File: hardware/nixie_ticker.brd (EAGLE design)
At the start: 127 x 61 mm, 78 parts, among them Q1 BCX19SMD, Q2 BCX19SMD, U1 K155ID1, U2 K155ID1, U3 K155ID1, U4 K155ID1, U5 K155ID1, U6 K155ID1

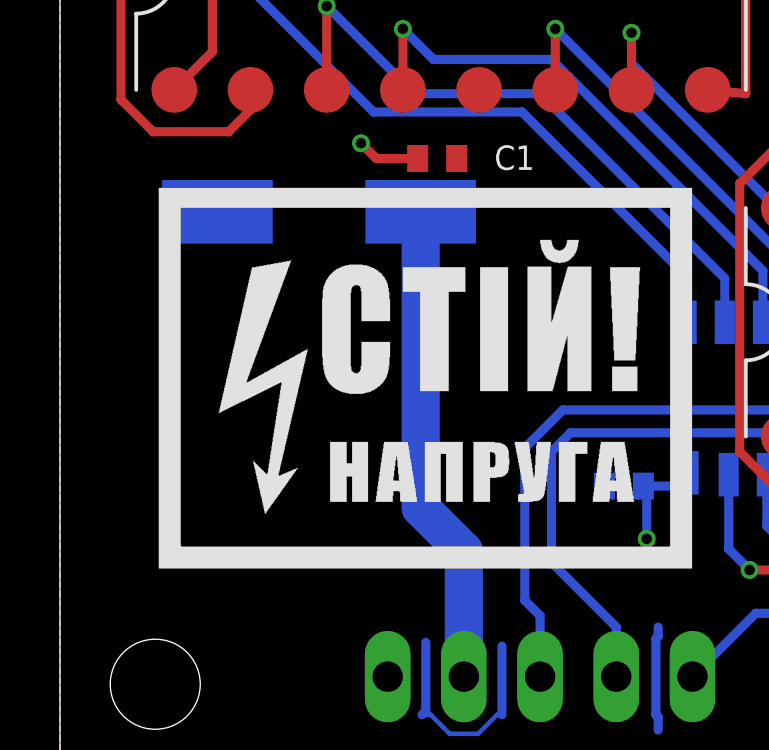
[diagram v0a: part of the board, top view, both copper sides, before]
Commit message: Changing OSH logo on power supply
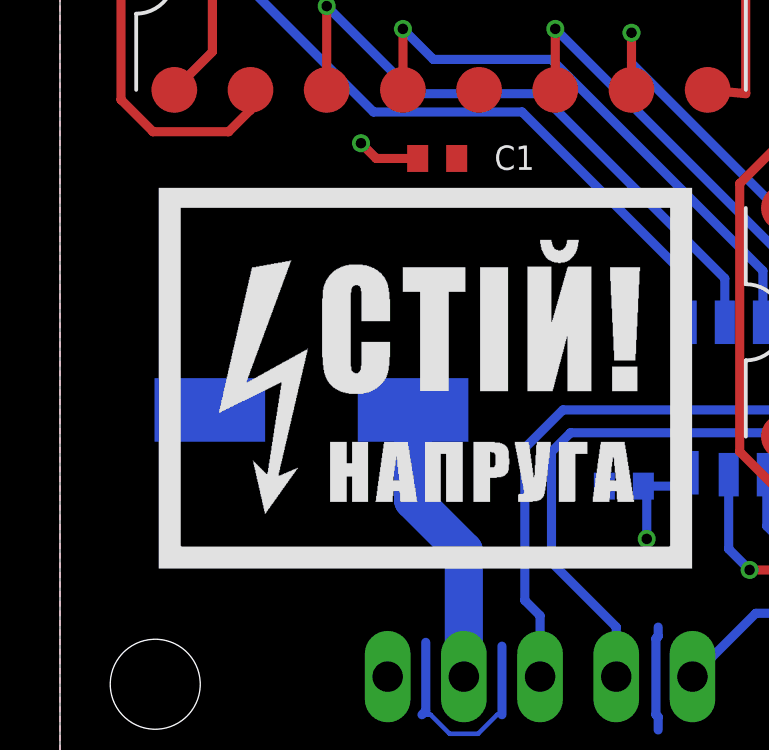
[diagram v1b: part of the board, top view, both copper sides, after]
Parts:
- moved C15 6.61 mm to (8.38, 12.3)
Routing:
- net +5V: track 38.8 -> 32.3 mm
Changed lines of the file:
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@@
 <attribute name="VALUE" x="80.01" y="5.207" size="1.27" layer="28" rot="MR90"/>
 </element>
-<element name="C15" library="nixie_ticker" library_urn="urn:adsk.eagle:library:3857935" package="CAPAE830X1050" package3d_urn="urn:adsk.eagle:package:3945414/1" value="220uF" x="8.636" y="18.923" rot="MR0"/>
+<element name="C15" library="nixie_ticker" library_urn="urn:adsk.eagle:library:3857935" package="CAPAE830X1050" package3d_urn="urn:adsk.eagle:package:3945414/1" value="220uF" x="8.382" y="12.319" rot="MR0"/>
 <element name="JP2" library="pinhead" library_urn="urn:adsk.eagle:library:325" package="1X05" package3d_urn="urn:adsk.eagle:package:22469/2" value="" x="16.002" y="3.429" smashed="yes" rot="MR180">
 <attribute name="VALUE" x="9.652" y="6.604" size="1.27" layer="28" rot="MR180"/>
@@
 <contactref element="C15" pad="1"/>
 <contactref element="JP2" pad="2"/>
-<wire x1="12.0237" y1="18.923" x2="12.0237" y2="9.0583" width="1.27" layer="16"/>
+<wire x1="11.7697" y1="12.319" x2="11.7697" y2="9.3123" width="1.27" layer="16"/>
 <wire x1="13.462" y1="7.62" x2="13.462" y2="3.429" width="1.27" layer="16"/>
-<wire x1="12.0237" y1="9.0583" x2="13.462" y2="7.62" width="1.27" layer="16"/>
+<wire x1="11.7697" y1="9.3123" x2="13.462" y2="7.62" width="1.27" layer="16"/>
 <wire x1="71.755" y1="10.225" x2="70.674" y2="9.144" width="0.3048" layer="16"/>
 <wire x1="69.992" y1="9.144" x2="68.468" y2="10.668" width="0.3048" layer="16"/>

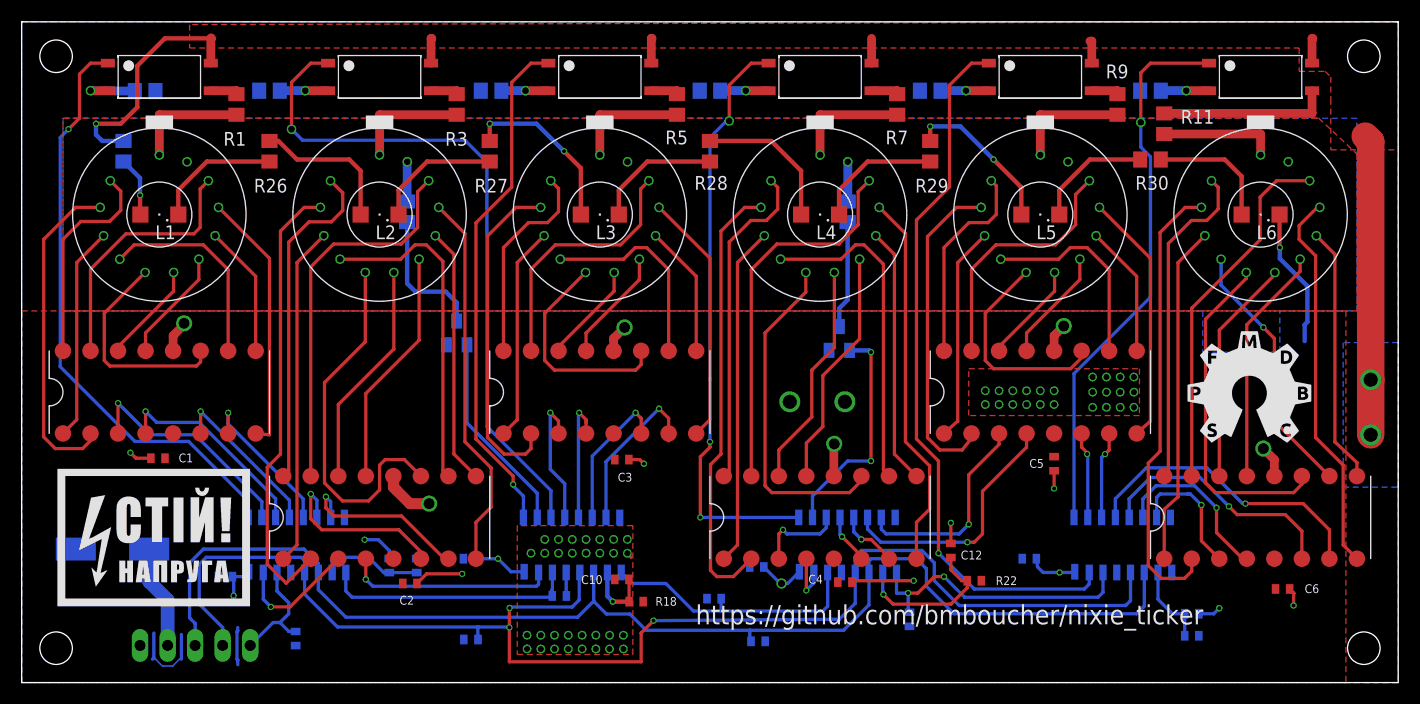
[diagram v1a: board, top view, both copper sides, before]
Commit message: Updates 8-17, adding fifth shift register
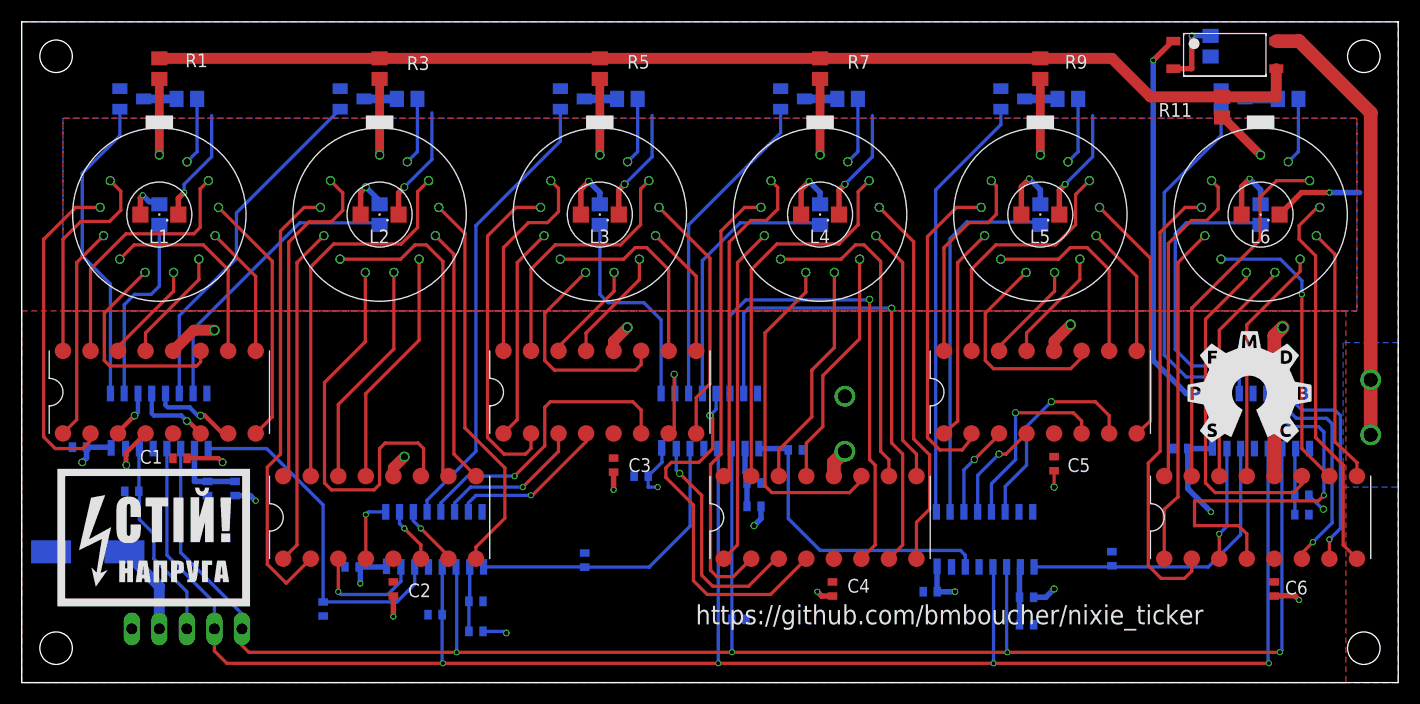
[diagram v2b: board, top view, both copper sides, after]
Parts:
- removed U$14, U$18, U$21, U$22, U$23: TLP3873D, nixie_ticker:SOP254P1000X215-4
- added C16, C17: (no value), resistor:C0402
- added Q3, Q4, Q5, Q6: BCX19SMD, transistor-npn:SOT23-BEC
- added R31: (no value), resistor:R0402
- added U$1: 74AHC595, nixie_ticker:16SOIC
- R12: device resistor:R0805 -> resistor:R0402
- moved R2 98.4 mm to (109.7, 58.7), turned to 90 degrees
- moved U$13 98.3 mm to (111.0, 57.9)
- moved R12 39.9 mm to (118.1, 17.3)
- moved R10 33.0 mm to (116.8, 53.8)
- moved R8 33.0 mm to (96.5, 53.8)
- moved Q1 23.6 mm to (30.5, 53.8), turned to 90 degrees
- moved Q2 22.5 mm to (71.1, 53.8), turned to 90 degrees
- moved R17 21.8 mm to (27.8, 6.79), turned to 90 degrees
- moved R22 21.4 mm to (67.6, 16.3), flipped to the bottom, turned to 180 degrees
- moved C8 20.6 mm to (17.1, 17.9), turned to 270 degrees
- moved R16 20.3 mm to (10.2, 17.7), turned to 180 degrees
- moved C12 19.2 mm to (67.6, 18.4), flipped to the bottom, turned to 180 degrees
- moved R23 18.8 mm to (71.4, 21.5), turned to 0 degrees
- moved C7 18.0 mm to (5.33, 21.7)
- moved U$3 17.1 mm to (12.7, 24.1)
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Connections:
- removed net D1A: U$13.1, U$3.P$1
- removed net D2A: U$14.1, U$4.P$3
- removed net D3A: U$18.1, U$4.P$1
- removed net D4A: U$21.1, U$9.P$1
- removed net D5A: U$10.P$15, U$22.1
- removed net D6A: U$10.P$1, U$23.1
- removed net N$106: R3.2, U$14.3
- removed net N$107: R4.2, U$14.2
- removed net N$112: R5.2, U$18.3
- removed net N$113: R6.2, U$18.2
- removed net N$119: R7.2, U$21.3
- removed net N$120: R8.2, U$21.2
- removed net N$146: R9.2, U$22.3
- removed net N$147: R10.2, U$22.2
- removed net N$153: R11.2, U$23.3
- removed net N$154: R12.2, U$23.2
- removed net N$28: L3.C, R28.1
- removed net N$41: L4.C, R29.2
- removed net N$43: L5.C, R30.1
- new net ANODE: U$1.P$1, U$13.1
- new net D1PR: Q3.B, U$3.P$1
- new net D3PR: Q4.B, U$4.P$4
- new net D5PR: Q5.B, U$10.P$1
- new net D6PR: Q6.B, U$1.P$2
- new net L1: R25.2, U$3.P$2
- new net L2: R26.1, U$3.P$7
- new net L3: R27.2, U$9.P$1
- new net L4: R28.1, U$9.P$4
- new net L5: R29.2, U$10.P$2
- new net L6: R30.1, U$1.P$3
- new net N$45: N1.P$2, R4.2
- new net N$46: Q3.C, R4.1
- new net N$47: N3.P$2, R6.2
- new net N$48: Q4.C, R6.1
- new net N$49: N5.P$2, R8.2
- new net N$50: Q5.C, R8.1
- new net N$51: N6.P$2, R10.2
- new net N$52: Q6.C, R10.1
- net +5V: now also C17.1, R12.2, U$1.P$16
- net CLK: now also U$1.P$12
- net D1I1: now also U$3.P$3; no longer U$3.P$2
- net D1I8: now also U$3.P$15; no longer U$3.P$3
- net D2I1: now also U$4.P$15; no longer U$3.P$15
- net D2I2: now also U$4.P$2; no longer U$3.P$6
- net D2I4: now also U$4.P$3; no longer U$3.P$7
- net D2I8: now also U$4.P$1; no longer U$4.P$15
- net D2PR: now also U$3.P$6; no longer U$4.P$2
- net D3I1: now also U$4.P$6; no longer U$4.P$4
- net D3I2: now also U$4.P$5; no longer U$4.P$6
- net D3I4: now also U$9.P$2; no longer U$4.P$7
- net D3I8: now also U$4.P$7; no longer U$4.P$5
- net D4I1: now also U$9.P$15; no longer U$9.P$3
- net D4I2: now also U$9.P$6; no longer U$9.P$4
- net D4I4: now also U$9.P$7; no longer U$9.P$5
- net D4I8: now also U$9.P$5; no longer U$9.P$15
- net D4PR: now also U$9.P$3; no longer U$9.P$2
- net D5I1: now also U$10.P$3; no longer U$9.P$7
- net D5I2: now also U$10.P$5; no longer U$10.P$2
- net D5I4: now also U$10.P$6; no longer U$10.P$3
- net D5I8: now also U$10.P$4; no longer U$9.P$6
- net D6I1: now also U$1.P$15; no longer U$10.P$7
- net D6I2: now also U$1.P$6; no longer U$10.P$5
- net D6I4: now also U$1.P$7; no longer U$10.P$4
- net D6I8: now also U$1.P$5; no longer U$10.P$6
- net DATA: now also JP2.3; no longer JP2.5
- net GND: now also C16.2, C17.2, L1.C, L2.C, L3.C, L4.C, L5.C, Q3.E, Q4.E, Q5.E, Q6.E, R31.1, U$1.P$13, U$1.P$8; no longer R10.1, R12.1, R4.1, R6.1, R8.1
- net LATCH: now also JP2.5, U$1.P$11; no longer JP2.3
- net N$102: now also R11.2, R3.2, R5.2, R7.2, R9.2
- net N$24: now also R31.2, U$1.P$14, U$10.P$9; no longer L1.C, R26.1
- net N$26: now also C16.1, R12.1, U$1.P$10; no longer L2.C, R27.2
- net V+: no longer R25.2, U$14.4, U$18.4, U$21.4, U$22.4, U$23.4
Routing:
- net N$102: track 2.68 -> 107.1 mm
- net D5A: track 66.3 -> 0.00 mm, vias 1 -> 0
- net D2A: track 62.9 -> 0.00 mm, vias 1 -> 0
- net D1A: track 54.7 -> 0.00 mm, vias 1 -> 0
- net D4A: track 54.7 -> 0.00 mm, vias 3 -> 0
- net LATCH: track 117.5 -> 170.1 mm, vias 0 -> 4
- net D6A: track 51.0 -> 0.00 mm, vias 1 -> 0
- net D3A: track 47.4 -> 0.00 mm, vias 1 -> 0
- net CLK: track 129.2 -> 175.9 mm, vias 3 -> 4
- net D3PR: track 0.00 -> 42.2 mm
- net D4I2: track 4.63 -> 45.4 mm
- net D5PR: track 0.00 -> 39.7 mm
- net D4I4: track 5.85 -> 45.3 mm
- net GND: track 64.8 -> 102.6 mm, vias 69 -> 17
- net ANODE: track 0.00 -> 37.3 mm, vias 0 -> 1
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- removed copper zone on layer 1, net GND
- removed copper zone on layer 1, net V+
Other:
- board text added: "+"
- board text added: "-"
- board text removed: "00 D6 1 08 D5 1 16 D3 4 24 D2 4 01 D6 8 09 D5 8 17 D3 2 25 D2 2 02 D6 2 10 D4 4 18 D3 8 26 D1 4 03 D6 4 11 D4 2 19 D3 1 27 D1 2 04 D5 4 12 D4 1 20 D2 A 28 D1 8 05 D5 2 13 D4 P 21 D2 P 29 D1 1 06 D6 A 14 D4 A 22 D3 A 30 D1 A 07 D5 A 15 D4 8 23 D2 8 31 D2 1"
- board text removed: "5V"

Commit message: Updates to BOM
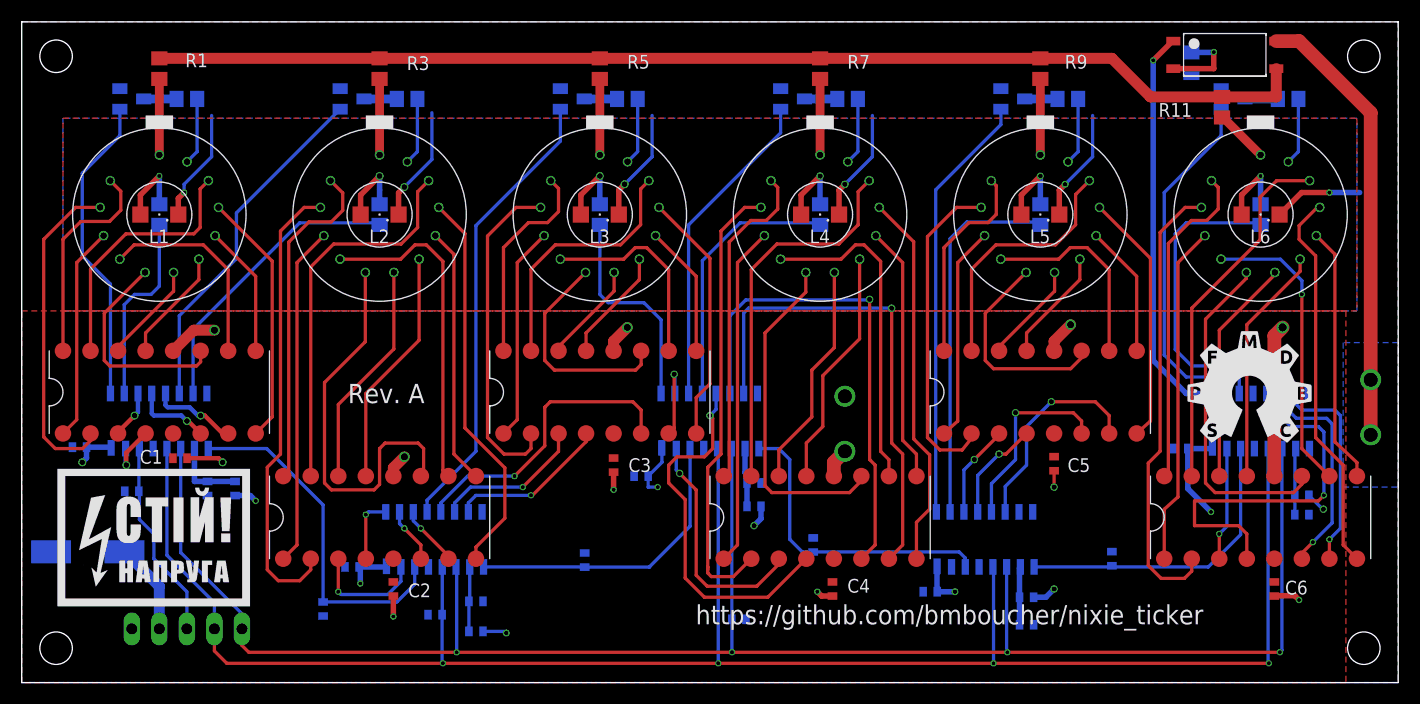
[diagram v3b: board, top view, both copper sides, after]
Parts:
- moved R23 8.92 mm to (73.0, 12.7), turned to 270 degrees
- moved R2 2.34 mm to (107.9, 57.2)
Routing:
- net N$29: track 3.67 -> 6.89 mm
- net N$25: track 4.85 -> 6.89 mm
- net N$30: track 5.87 -> 6.89 mm
- net N$27: track 5.87 -> 6.89 mm
- net N$103: track 6.52 -> 7.34 mm
- net N$20: track 41.5 -> 42.2 mm
- net D4I1: track 21.2 -> 21.8 mm
- net N$70: track 41.2 -> 41.7 mm
- net N$44: track 6.38 -> 6.89 mm
- net N$42: track 6.38 -> 6.89 mm
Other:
- board text added: "00 D1 8 01 D1 P 02 L1 03 D1 1 04 D1 2 05 D1 4 06 D2 P 07 L2"
- board text added: "08 D2 1 09 D2 8 10 D2 2 11 D2 4 12 D3 P 13 D3 2 14 D3 1 15 D3 8"
- board text added: "16 D4 1 17 L3 18 D3 4 19 D4 P 20 L4 21 D4 8 22 D4 2 23 D4 4"
- board text added: "24 25 D5 P 26 L5 27 D5 1 28 D5 8 29 D5 2 30 D5 4 31"
- board text added: "32 D6 1 33 ANODE 34 D6 P 35 L6 36 37 D6 8 38 D6 2 39 D6 4"
- board text added: "Rev. A"

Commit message: Final update before submitting to PCB shop
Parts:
- removed L1, L2, L3, L4, L5, L6: (no value), led:SML1206
- removed U$13: TLP3873D, nixie_ticker:SOP254P1000X215-4
- removed U$17: ZKFDS, nixie_ticker:ZKFDS
- added JP1: (no value), pinhead:1X05
- added LED1, LED2, LED3, LED4, LED5, LED6: (no value), led:CHIP-LED0603
- added U7: K155ID1, nixie_ticker:DIP-16_SMD
- C1, C2, C3, C4, C5, C6: value (none) -> 1uF
- C15: value 220uF -> (none); device nixie_ticker:CAPAE830X1050 -> resistor:C0402
- C17: value (none) -> 220uF; device resistor:C0402 -> nixie_ticker:CAPAE830X1050
- JP2: value (none) -> ZKFDS; device pinhead:1X05 -> nixie_ticker:ZKFDS
- R1, R2, R3, R4, R5, R6: value (none) -> 22k; device resistor:R0805 -> resistor:R1206
- R10, R11, R13, R20, R23, R8, R9: value (none) -> 10k
- R12: value (none) -> 10k; device resistor:R0402 -> resistor:R0805
- R15, R16, R17, R18, R19: device resistor:R0402 -> resistor:R0805
- R21, R22, R24, R31: value (none) -> 100k
- R25, R27, R29: value (none) -> 10k; device resistor:R0805 -> resistor:R0402
- R26, R28, R30: value (none) -> 100k; device resistor:R0805 -> resistor:R0402
- R7: value (none) -> 750; device resistor:R0805 -> resistor:R0603
- U1: value K155ID1 -> TLP3873D; device nixie_ticker:DIP-16_SMD -> nixie_ticker:SOP254P1000X215-4
- moved JP2 110.7 mm to (124.5, 22.9), turned to 0 degrees
- moved U1 107.0 mm to (115.6, 56.1), turned to 180 degrees
- moved C17 101.3 mm to (6.10, 12.1)
- moved R30 84.6 mm to (38.1, 6.26), turned to 180 degrees
- moved R13 81.3 mm to (116.8, 53.8)
- moved R8 81.3 mm to (15.2, 53.8)
- moved R2 74.9 mm to (33.0, 55.4), flipped to the top
- moved R18 64.7 mm to (94.0, 43.2), turned to 270 degrees
- moved R14 64.4 mm to (12.7, 43.2), turned to 270 degrees
- moved C15 61.8 mm to (67.6, 18.4), turned to 180 degrees
- moved R25 61.1 mm to (67.6, 16.3), turned to 180 degrees
- moved R10 61.0 mm to (55.9, 53.8)
- moved R19 60.9 mm to (114.3, 43.2), turned to 90 degrees
- moved R17 58.5 mm to (73.7, 43.2)
- moved R9 58.5 mm to (35.6, 53.8), flipped to the bottom, turned to 180 degrees
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- renumbered U$1 to U12, U$10 to U11, U$24 to JP3, U$3 to U8, U$4 to U9, U$9 to U10
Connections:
- net +5V: now also C10.1, C8.1, JP1.2, R20.2, R23.2, R25.2, R27.2, R29.2, U7.P$5; no longer C13.1, C15.1, JP2.2, R12.2, R15.2, R18.2, R22.2, R24.2, U1.P$5
- net ANODE: now also U1.1, U12.P$3; no longer U$13.1, U12.P$1
- net CLK: now also JP1.4, R30.2; no longer JP2.4, R20.2
- net D1I1: now also U2.P$3; no longer U1.P$3
- net D1I2: now also U2.P$6; no longer U1.P$6
- net D1I4: now also U2.P$7; no longer U1.P$7
- net D1I8: now also U2.P$4; no longer U1.P$4
- net D1PR: now also Q1.B; no longer Q3.B
- net D2I1: now also U3.P$3; no longer U2.P$3
- net D2I2: now also U3.P$6; no longer U2.P$6
- net D2I4: now also U3.P$7; no longer U2.P$7
- net D2I8: now also U3.P$4; no longer U2.P$4
- net D2PR: now also Q2.B; no longer Q1.B
- net D3I1: now also U4.P$3; no longer U3.P$3
- net D3I2: now also U4.P$6; no longer U3.P$6
- net D3I4: now also U4.P$7; no longer U3.P$7
- net D3I8: now also U4.P$4; no longer U3.P$4
- net D3PR: now also Q3.B; no longer Q4.B
- net D4I1: now also U5.P$3; no longer U4.P$3
- net D4I2: now also U5.P$6; no longer U4.P$6
- net D4I4: now also U5.P$7; no longer U4.P$7
- net D4I8: now also U5.P$4; no longer U4.P$4
- net D4PR: now also Q4.B; no longer Q2.B
- net D5I1: now also U6.P$3; no longer U5.P$3
- net D5I2: now also U6.P$6; no longer U5.P$6
- net D5I4: now also U6.P$7; no longer U5.P$7
- net D5I8: now also U6.P$4; no longer U5.P$4
- net D6I1: now also U7.P$3; no longer U6.P$3
- net D6I2: now also U7.P$6; no longer U6.P$6
- net D6I4: now also U7.P$7; no longer U6.P$7
- net D6I8: now also U7.P$4; no longer U6.P$4
- net D6PR: now also U12.P$1; no longer U12.P$2
- net DATA: now also JP1.3, R21.2; no longer JP2.3, R16.2
- net GND: now also JP1.1, LED1.C, LED2.C, LED3.C, LED4.C, LED5.C, LED6.C, R22.1, R24.1, R26.1, R28.1, R30.1, R7.1, U7.P$12; no longer JP2.1, L1.C, L2.C, L3.C, L4.C, L5.C, L6.C, R16.1, R17.1, R19.1, R2.1, R20.1, R23.1, U1.P$12
- net L1: now also R14.2; no longer R25.2
- net L2: now also R15.1; no longer R26.1
- net L3: now also R16.2; no longer R27.2
- net L4: now also R17.1; no longer R28.1
- net L5: now also R18.2; no longer R29.2
- net L6: now also R19.1, U12.P$2; no longer R30.1, U12.P$3
- net LATCH: now also JP1.5, R31.2; no longer JP2.5, R19.2
- net N$1: now also U2.P$16; no longer U1.P$16
- net N$10: now also U2.P$2; no longer U1.P$2
- net N$100: now also U6.P$2; no longer U5.P$2
- net N$102: now also R2.2, R4.2, R6.2, U1.3; no longer R11.2, R7.2, R9.2, U$13.3
- net N$103: now also R7.2, U1.2; no longer R2.2, U$13.2
- net N$104: now also R6.1; no longer R11.1
- net N$105: now also R2.1; no longer R3.1
- net N$108: now also C14.1, R23.1; no longer C10.1, R18.1
- net N$109: now also C12.1, R20.1; no longer C8.1, R15.1
- net N$11: now also U3.P$16; no longer U2.P$16
- net N$110: now also C15.1, R25.1; no longer C12.1, R22.1
- net N$111: now also C16.1, R27.1; no longer C14.1, R24.1
- net N$118: now also R3.1; no longer R5.1
- net N$12: now also U3.P$15; no longer U2.P$15
- net N$121: now also U7.P$16; no longer U6.P$16
- net N$122: now also U7.P$15; no longer U6.P$15
- net N$123: now also U7.P$8; no longer U6.P$8
- net N$124: now also U7.P$9; no longer U6.P$9
- net N$125: now also U7.P$13; no longer U6.P$13
- net N$126: now also U7.P$14; no longer U6.P$14
- net N$127: now also U7.P$11; no longer U6.P$11
- net N$128: now also U7.P$10; no longer U6.P$10
- net N$129: now also U7.P$1; no longer U6.P$1
- net N$13: now also U3.P$8; no longer U2.P$8
- net N$130: now also U7.P$2; no longer U6.P$2
- net N$14: now also U3.P$9; no longer U2.P$9
- net N$145: now also R4.1; no longer R7.1
- net N$15: now also U3.P$13; no longer U2.P$13
- net N$16: now also U3.P$14; no longer U2.P$14
- net N$160: now also Q2.C, R9.1; no longer Q1.C, R13.1
- net N$161: now also Q4.C, R11.1; no longer Q2.C, R14.1
- net N$162: now also R11.2; no longer R14.2
- net N$163: now also R9.2; no longer R13.2
- net N$17: now also U3.P$11; no longer U2.P$11
- net N$18: now also U3.P$10; no longer U2.P$10
- net N$19: now also U3.P$1; no longer U2.P$1
- net N$2: now also U2.P$15; no longer U1.P$15
- net N$20: now also U3.P$2; no longer U2.P$2
- net N$21: now also R24.2; no longer R21.2
- net N$22: now also R22.2; no longer R17.2
- net N$23: now also R26.2; no longer R23.2
- net N$24: now also R28.2; no longer R31.2
- net N$25: now also LED2.A, R15.2; no longer L2.A, R26.2
- net N$26: now also C13.1, R29.1; no longer C16.1, R12.1
- net N$27: now also LED3.A, R16.1; no longer L3.A, R27.1
- net N$29: now also LED1.A, R14.1; no longer L1.A, R25.1
- net N$3: now also U2.P$8; no longer U1.P$8
- net N$30: now also LED4.A, R17.2; no longer L4.A, R28.2
- net N$31: now also U4.P$16; no longer U3.P$16
- net N$32: now also U4.P$15; no longer U3.P$15
- net N$33: now also U4.P$8; no longer U3.P$8
- net N$34: now also U4.P$9; no longer U3.P$9
- net N$35: now also U4.P$13; no longer U3.P$13
- net N$36: now also U4.P$14; no longer U3.P$14
- net N$37: now also U4.P$11; no longer U3.P$11
- net N$38: now also U4.P$10; no longer U3.P$10
- net N$39: now also U4.P$1; no longer U3.P$1
- net N$4: now also U2.P$9; no longer U1.P$9
- net N$40: now also U4.P$2; no longer U3.P$2
- net N$42: now also LED5.A, R18.1; no longer L5.A, R29.1
- net N$44: now also LED6.A, R19.2; no longer L6.A, R30.2
- net N$45: now also R8.2; no longer R4.2
- net N$46: now also Q1.C, R8.1; no longer Q3.C, R4.1
- net N$47: now also R10.2; no longer R6.2
- net N$48: now also Q3.C, R10.1; no longer Q4.C, R6.1
- net N$49: now also R12.2; no longer R8.2
- net N$5: now also U2.P$13; no longer U1.P$13
- net N$50: now also R12.1; no longer R8.1
- net N$51: now also R13.2; no longer R10.2
- net N$52: now also R13.1; no longer R10.1
- net N$6: now also U2.P$14; no longer U1.P$14
- net N$61: now also U5.P$16; no longer U4.P$16
- net N$62: now also U5.P$15; no longer U4.P$15
- net N$63: now also U5.P$8; no longer U4.P$8
- net N$64: now also U5.P$9; no longer U4.P$9
- net N$65: now also U5.P$13; no longer U4.P$13
- net N$66: now also U5.P$14; no longer U4.P$14
- net N$67: now also U5.P$11; no longer U4.P$11
- net N$68: now also U5.P$10; no longer U4.P$10
- net N$69: now also U5.P$1; no longer U4.P$1
- net N$7: now also U2.P$11; no longer U1.P$11
- net N$70: now also U5.P$2; no longer U4.P$2
- net N$8: now also U2.P$10; no longer U1.P$10
- net N$9: now also U2.P$1; no longer U1.P$1
- net N$90: now also R5.1; no longer R9.1
- net N$91: now also U6.P$16; no longer U5.P$16
- net N$92: now also U6.P$15; no longer U5.P$15
- net N$93: now also U6.P$8; no longer U5.P$8
- net N$94: now also U6.P$9; no longer U5.P$9
- net N$95: now also U6.P$13; no longer U5.P$13
- net N$96: now also U6.P$14; no longer U5.P$14
- net N$97: now also U6.P$11; no longer U5.P$11
- net N$98: now also U6.P$10; no longer U5.P$10
- net N$99: now also U6.P$1; no longer U5.P$1
- net V+: now also JP2.P$1, JP2.P$2, U1.4; no longer U$13.4, U$17.P$1, U$17.P$2
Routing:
- net N$102: track 107.1 -> 0.07 mm
- net N$104: track 4.99 -> 11.8 mm
- net N$103: track 7.34 -> 12.8 mm
- net ANODE: track 37.3 -> 42.4 mm
- net GND: track 102.6 -> 105.8 mm
- net N$122: track 33.5 -> 36.4 mm
- net N$90: track 7.01 -> 5.27 mm
- net N$57: track 7.01 -> 5.27 mm
- net N$145: track 7.01 -> 5.27 mm
- net N$118: track 7.01 -> 5.27 mm
- net N$105: track 7.01 -> 5.27 mm
- net N$44: track 6.89 -> 5.20 mm
- net D6PR: track 32.7 -> 31.3 mm
- net L6: track 27.5 -> 26.4 mm
- added copper zone on layer 1, net N$102
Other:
- board text added: "32 D6 1 32 D6 P 34 L6 35 ANODE 36 37 D6 8 38 D6 2 39 D6 4"
- board text removed: "32 D6 1 33 ANODE 34 D6 P 35 L6 36 37 D6 8 38 D6 2 39 D6 4"

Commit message: Updates 8-28
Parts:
- C1, C2, C3, C4, C5, C6: device resistor:C0402 -> nixie_ticker:C0402
- C10, C11, C12, C13, C14, C15, C16, C7, C8, C9: value (none) -> C0402; device resistor:C0402 -> nixie_ticker:C0402
- R20, R21, R22, R23, R24, R25, R26, R27, R28, R29, R30, R31: device resistor:R0402 -> nixie_ticker:R0402
